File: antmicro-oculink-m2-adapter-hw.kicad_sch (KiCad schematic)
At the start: 10 parts, among them J1 OCuLink_x4_Amphenol_G14A42121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, J2 PCB-Edge_M.2_Key-M

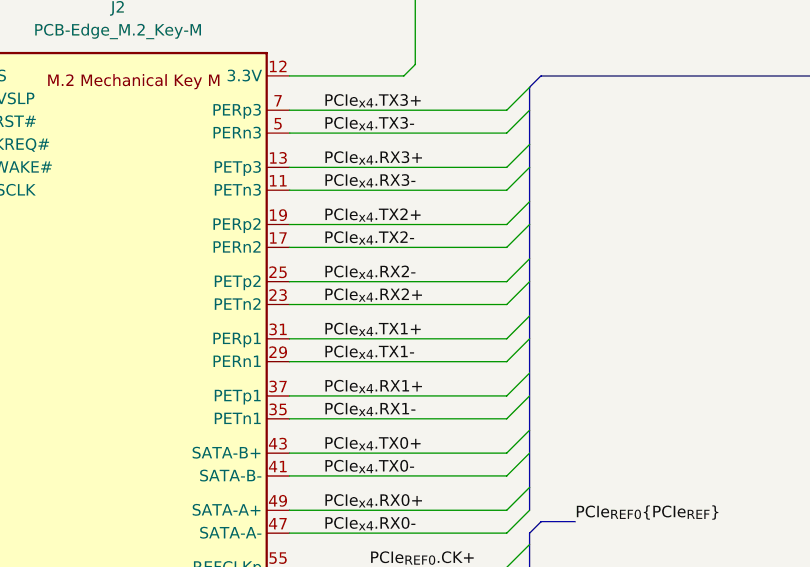
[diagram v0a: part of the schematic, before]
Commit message: [#79281] Fix lane polarity
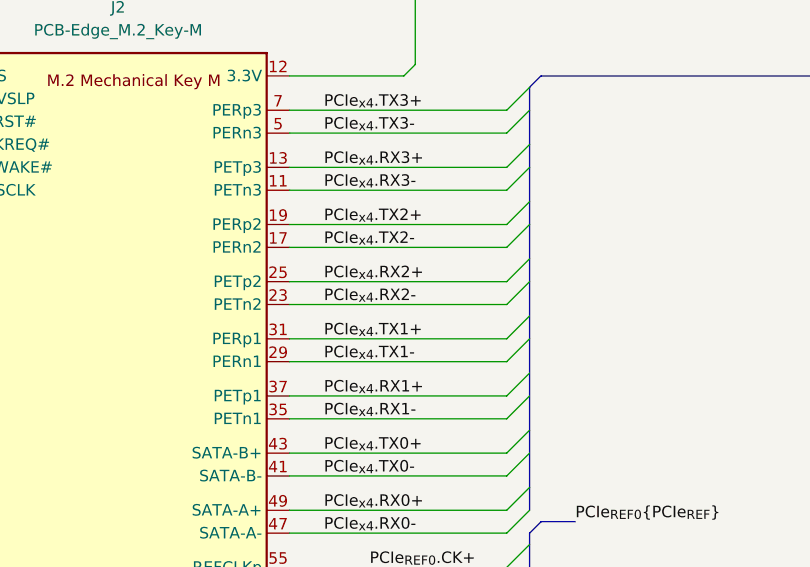
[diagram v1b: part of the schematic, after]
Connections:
- net PCIe_{x4}.RX2+: now also J2.25 (PETp2); no longer J2.23 (PETn2)
- net PCIe_{x4}.RX2-: now also J2.23 (PETn2); no longer J2.25 (PETp2)
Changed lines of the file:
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@@
-		)
-	)
-	(label "PCIe_{x4}.RX2-"
-		(at 97.79 105.41 0)
-		(effects
-			(font
-				(size 1.27 1.27)
-			)
-			(justify left bottom)
 		)
 	)
@@
 			)
 			(justify right bottom)
-		)
-	)
-	(label "PCIe_{x4}.RX2+"
-		(at 97.79 107.95 0)
-		(effects
-			(font
-				(size 1.27 1.27)
-			)
-			(justify left bottom)
 		)
 	)
@@
 		(effects
 			(font
+				(size 1.27 1.27)
+			)
+			(justify left bottom)
+		)
+	)
+	(label "PCIe_{x4}.RX2-"
+		(at 97.79 107.95 0)
+		(effects
+			(font
+				(size 1.27 1.27)
+			)
+			(justify left bottom)
+		)
+	)
+	(label "PCIe_{x4}.RX2+"
+		(at 97.79 105.41 0)
+		(effects
+			(font
